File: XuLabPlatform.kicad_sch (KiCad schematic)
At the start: 0 parts

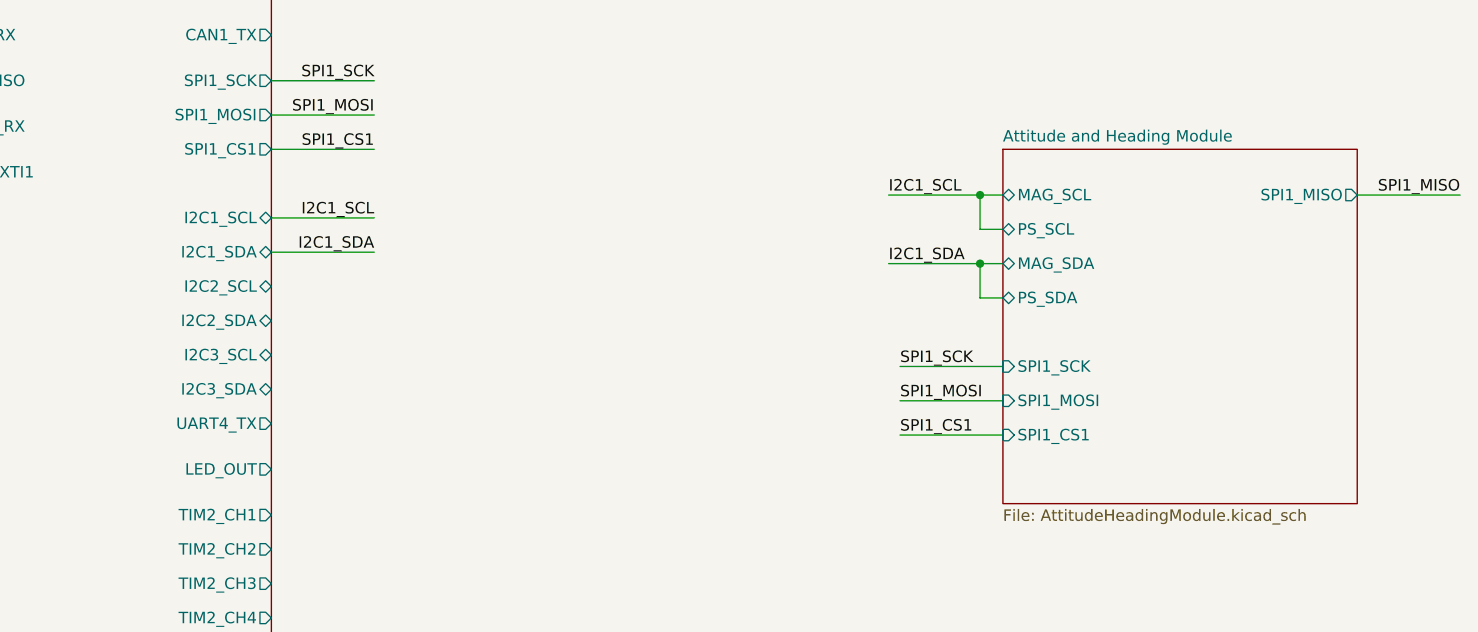
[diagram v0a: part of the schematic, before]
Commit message: Change magnetometer interface from I2C to SPI
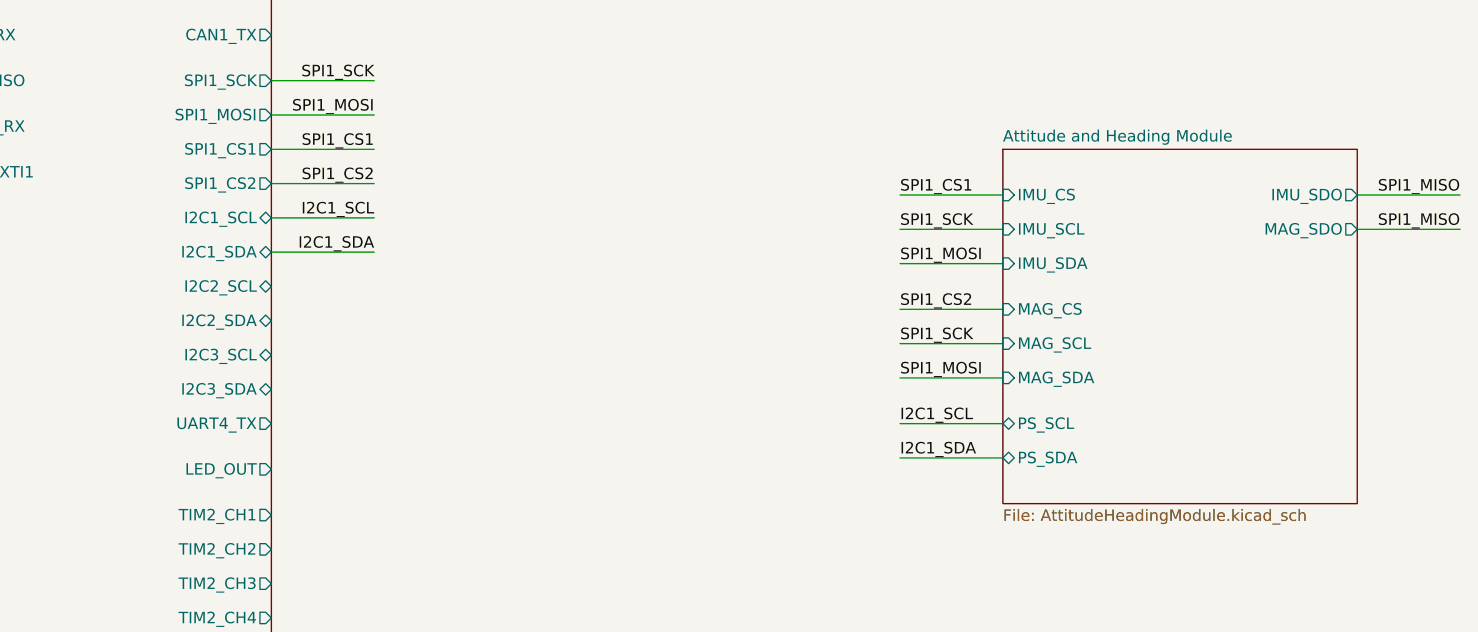
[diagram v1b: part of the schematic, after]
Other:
- sheet Attitude and Heading Module ports: added IMU_CS, IMU_SCL, IMU_SDA, IMU_SDO, MAG_CS, MAG_SDO; removed SPI1_CS1, SPI1_MISO, SPI1_MOSI, SPI1_SCK
- sheet MCU A ports: added SPI1_CS2; removed none
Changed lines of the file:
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@@
 	(title_block
 		(title "Main Sheet")
-		(date "2025-10-21")
+		(date "2025-10-23")
 		(rev "A")
 		(company "CU Boulder Senior Design Team 29 - Xu Lab")
 	)
-	(junction
-		(at 167.64 60.96)
-		(diameter 0)
-		(color 0 0 0 0)
-	)
-	(junction
-		(at 167.64 68.58)
-		(diameter 0)
-		(color 0 0 0 0)
+	(wire
+		(pts
+			(xy 158.75 64.77) (xy 170.18 64.77)
+		)
+		(stroke
+			(width 0)
+			(type default)
+		)
 	)
 	(wire
@@
 	(wire
 		(pts
+			(xy 209.55 64.77) (xy 220.98 64.77)
+		)
+		(stroke
+			(width 0)
+			(type default)
+		)
+	)
+	(wire
+		(pts
 			(xy 88.9 48.26) (xy 100.33 48.26)
 		)
@@
 	(wire
 		(pts
-			(xy 167.64 68.58) (xy 170.18 68.58)
-		)
-		(stroke
-			(width 0)
-			(type default)
-		)
-	)
-	(wire
-		(pts
-			(xy 170.18 72.39) (xy 167.64 72.39)
+			(xy 158.75 73.66) (xy 170.18 73.66)
 		)
 		(stroke
@@
 	(wire
 		(pts
-			(xy 170.18 64.77) (xy 167.64 64.77)
-		)
-		(stroke
-			(width 0)
-			(type default)
-		)
-	)
-	(wire
-		(pts
-			(xy 158.75 83.82) (xy 170.18 83.82)
-		)
-		(stroke
-			(width 0)
-			(type default)
-		)
-	)
-	(wire
-		(pts
-			(xy 167.64 60.96) (xy 167.64 64.77)
+			(xy 158.75 60.96) (xy 170.18 60.96)
+		)
+		(stroke
+			(width 0)
+			(type default)
+		)
+	)
+	(wire
+		(pts
+			(xy 158.75 68.58) (xy 170.18 68.58)
+		)
+		(stroke
+			(width 0)
+			(type default)
+		)
+	)
+	(wire
+		(pts
+			(xy 158.75 77.47) (xy 170.18 77.47)
 		)
 		(stroke
@@
 	(wire
 		(pts
-			(xy 158.75 80.01) (xy 170.18 80.01)
+			(xy 88.9 59.69) (xy 100.33 59.69)
 		)
 		(stroke
@@
 	(wire
 		(pts
-			(xy 157.48 60.96) (xy 167.64 60.96)
-		)
-		(stroke
-			(width 0)
-			(type default)
-		)
-	)
-	(wire
-		(pts
-			(xy 158.75 87.63) (xy 170.18 87.63)
-		)
-		(stroke
-			(width 0)
-			(type default)
-		)
-	)
-	(wire
-		(pts
-			(xy 157.48 68.58) (xy 167.64 68.58)
-		)
-		(stroke
-			(width 0)
-			(type default)
-		)
-	)
-	(wire
-		(pts
-			(xy 167.64 60.96) (xy 170.18 60.96)
-		)
-		(stroke
-			(width 0)
-			(type default)
-		)
-	)
-	(wire
-		(pts
 			(xy 209.55 60.96) (xy 220.98 60.96)
 		)
@@
 	(wire
 		(pts
-			(xy 167.64 68.58) (xy 167.64 72.39)
+			(xy 158.75 81.28) (xy 170.18 81.28)
+		)
+		(stroke
+			(width 0)
+			(type default)
+		)
+	)
+	(wire
+		(pts
+			(xy 158.75 90.17) (xy 170.18 90.17)
 		)
 		(stroke
@@
 		)
 	)
-	(label "SPI1_CS1"
-		(at 158.75 87.63 0)
-		(effects
-			(font
-				(size 1.27 1.27)
-			)
-			(justify left bottom)
+	(wire
+		(pts
+			(xy 158.75 86.36) (xy 170.18 86.36)
+		)
+		(stroke
+			(width 0)
+			(type default)
+		)
+	)
+	(label "SPI1_MOSI"
+		(at 158.75 81.28 0)
+		(effects
+			(font
+				(size 1.27 1.27)
+			)
+			(justify left bottom)
+		)
+	)
+	(label "SPI1_MISO"
+		(at 220.98 60.96 180)
+		(effects
+			(font
+				(size 1.27 1.27)
+			)
+			(justify right bottom)
 		)
 	)
@@
 	)
 	(label "SPI1_MISO"
-		(at 220.98 60.96 180)
+		(at 220.98 64.77 180)
 		(effects
 			(font
@@
 			)
 			(justify right bottom)
-		)
-	)
-	(label "I2C1_SDA"
-		(at 157.48 68.58 0)
-		(effects
-			(font
-				(size 1.27 1.27)
-			)
-			(justify left bottom)
 		)
 	)
@@
 		)
 	)
+	(label "SPI1_SCK"
+		(at 158.75 77.47 0)
+		(effects
+			(font
+				(size 1.27 1.27)
+			)
+			(justify left bottom)
+		)
+	)
 	(label "SPI1_MOSI"
 		(at 100.33 52.07 180)
@@
 		)
 	)
+	(label "SPI1_SCK"
+		(at 158.75 64.77 0)
+		(effects
+			(font
+				(size 1.27 1.27)
+			)
+			(justify left bottom)
+		)
+	)
+	(label "SPI1_CS1"
+		(at 158.75 60.96 0)
+		(effects
+			(font
+				(size 1.27 1.27)
+			)
+			(justify left bottom)
+		)
+	)
 	(label "I2C1_SCL"
-		(at 157.48 60.96 0)
-		(effects
-			(font
-				(size 1.27 1.27)
-			)
-			(justify left bottom)
+		(at 158.75 86.36 0)
+		(effects
+			(font
+				(size 1.27 1.27)
+			)
+			(justify left bottom)
+		)
+	)
+	(label "SPI1_CS2"
+		(at 100.33 59.69 180)
+		(effects
+			(font
+				(size 1.27 1.27)
+			)
+			(justify right bottom)
 		)
 	)
@@
 		)
 	)
+	(label "SPI1_CS2"
+		(at 158.75 73.66 0)
+		(effects
+			(font
+				(size 1.27 1.27)
+			)
+			(justify left bottom)
+		)
+	)
+	(label "I2C1_SDA"
+		(at 158.75 90.17 0)
+		(effects
+			(font
+				(size 1.27 1.27)
+			)
+			(justify left bottom)
+		)
+	)
 	(label ""
 		(at 97.79 48.26 0)
@@
 	)
 	(label "SPI1_SCK"
-		(at 158.75 80.01 0)
-		(effects
-			(font
-				(size 1.27 1.27)
-			)
-			(justify left bottom)
-		)
-	)
-	(label "SPI1_SCK"
 		(at 100.33 48.26 180)
 		(effects
@@
 	)
 	(label "SPI1_MOSI"
-		(at 158.75 83.82 0)
+		(at 158.75 68.58 0)
 		(effects
 			(font
@@
 			)
 		)
+		(pin "SPI1_CS2" output
+			(at 88.9 59.69 0)
+			(effects
+				(font
+					(size 1.27 1.27)
+				)
+				(justify right)
+			)
+		)
 		(instances
 			(project "XuLabPlatform"
@@
 			)
 		)
-		(pin "MAG_SCL" bidirectional
+		(pin "IMU_CS" input
 			(at 170.18 60.96 180)
 			(effects
@@
 			)
 		)
-		(pin "MAG_SDA" bidirectional
+		(pin "IMU_SCL" input
+			(at 170.18 64.77 180)
+			(effects
+				(font
+					(size 1.27 1.27)
+				)
+				(justify left)
+			)
+		)
+		(pin "IMU_SDA" input
 			(at 170.18 68.58 180)
 			(effects
@@
 			)
 		)
-		(pin "SPI1_CS1" input
-			(at 170.18 87.63 180)
-			(effects
-				(font
-					(size 1.27 1.27)
-				)
-				(justify left)
-			)
-		)
-		(pin "SPI1_MISO" output
+		(pin "IMU_SDO" output
 			(at 209.55 60.96 0)
 			(effects
@@
 			)
 		)
-		(pin "SPI1_MOSI" input
-			(at 170.18 83.82 180)
-			(effects
-				(font
-					(size 1.27 1.27)
-				)
-				(justify left)
-			)
-		)
-		(pin "SPI1_SCK" input
-			(at 170.18 80.01 180)
-			(effects
-				(font
-					(size 1.27 1.27)
-				)
-				(justify left)
+		(pin "MAG_CS" input
+			(at 170.18 73.66 180)
+			(effects
+				(font
+					(size 1.27 1.27)
+				)
+				(justify left)
+			)
+		)
+		(pin "MAG_SCL" input
+			(at 170.18 77.47 180)
+			(effects
+				(font
+					(size 1.27 1.27)
+				)
+				(justify left)
+			)
+		)
+		(pin "MAG_SDA" input
+			(at 170.18 81.28 180)
+			(effects
+				(font
+					(size 1.27 1.27)
+				)
+				(justify left)
+			)
+		)
+		(pin "MAG_SDO" output
+			(at 209.55 64.77 0)
+			(effects
+				(font
+					(size 1.27 1.27)
+				)
+				(justify right)
 			)
 		)
 		(pin "PS_SCL" bidirectional
-			(at 170.18 64.77 180)
+			(at 170.18 86.36 180)
 			(effects
 				(font
@@
 		)
 		(pin "PS_SDA" bidirectional
-			(at 170.18 72.39 180)
-			(effects
-				(font
+			(at 170.18 90.17 180)
+			(effects
+				(font

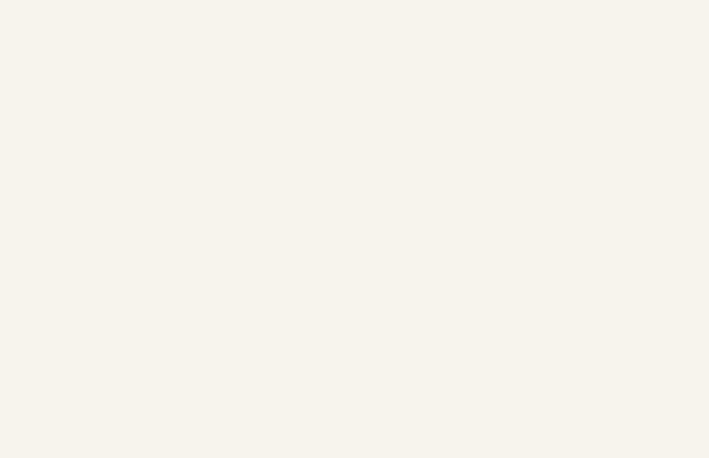
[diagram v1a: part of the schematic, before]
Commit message: Add power schematic sheet
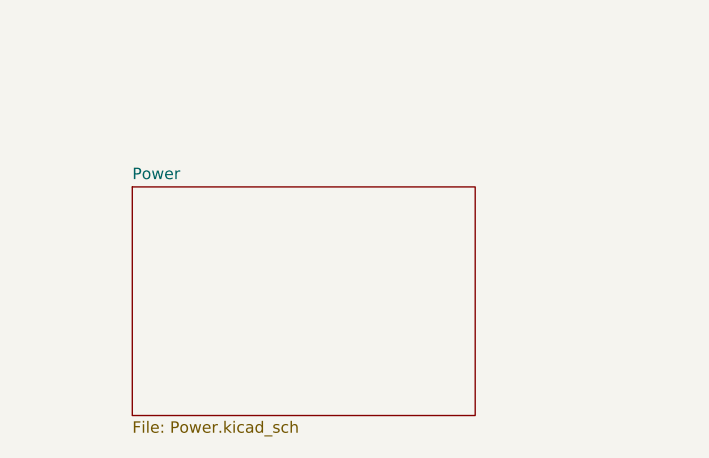
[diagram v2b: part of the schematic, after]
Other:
- added sheet Power (Power.kicad_sch)
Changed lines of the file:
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@@
+	)
+	(sheet
+		(at 50.8 152.4)
+		(size 38.1 25.4)
+		(exclude_from_sim no)
+		(in_bom yes)
+		(on_board yes)
+		(dnp no)
+		(fields_autoplaced yes)
+		(stroke
+			(width 0.1524)
+			(type solid)
+		)
+		(fill
+			(color 0 0 0 0.0000)
+		)
+		(property "Sheetname" "Power"
+			(at 50.8 151.6884 0)
+			(effects
+				(font
+					(size 1.27 1.27)
+				)
+				(justify left bottom)
+			)
+		)
+		(property "Sheetfile" "Power.kicad_sch"
+			(at 50.8 178.3846 0)
+			(effects
+				(font
+					(size 1.27 1.27)
+				)
+				(justify left top)
+			)
+		)
+		(instances
+			(project "XuLabPlatform"
+				(path "/71bb14ae-b730-4d22-a41d-cf68989dae2d"
+					(page "4")
+				)
+			)
+		)
 	)
 	(sheet

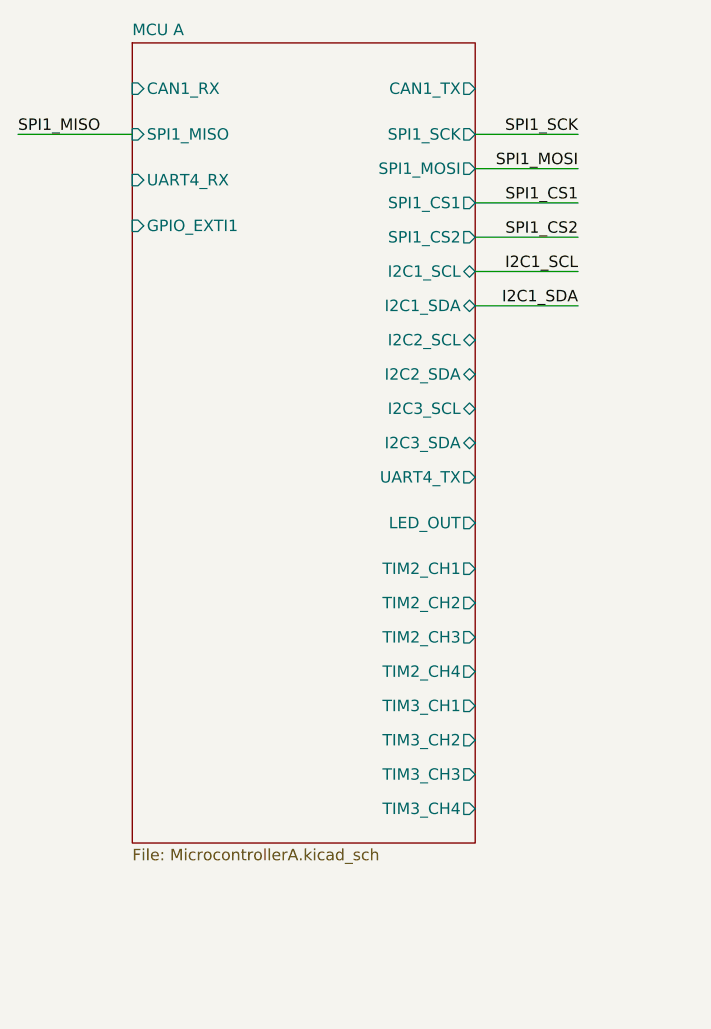
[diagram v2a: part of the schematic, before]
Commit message: Add indicator LED for MCU A
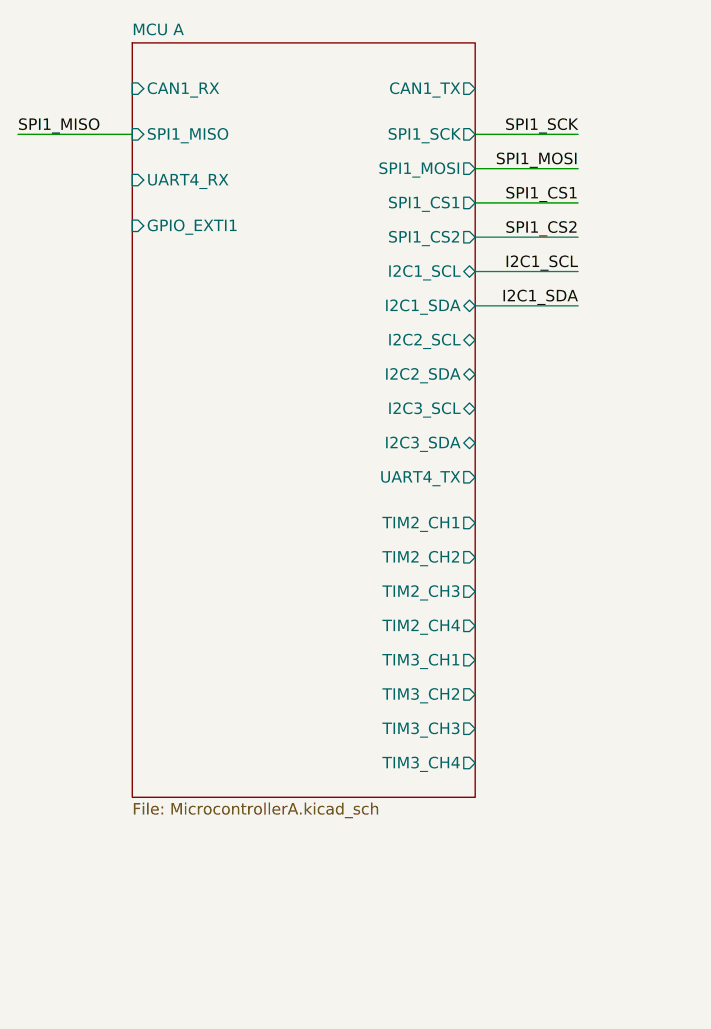
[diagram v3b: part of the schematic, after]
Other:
- sheet MCU A ports: added none; removed LED_OUT
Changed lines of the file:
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@@
 	(sheet
 		(at 50.8 38.1)
-		(size 38.1 88.9)
+		(size 38.1 83.82)
 		(exclude_from_sim no)
 		(in_bom yes)
@@
 		)
 		(property "Sheetfile" "MicrocontrollerA.kicad_sch"
-			(at 50.8 127.5846 0)
+			(at 50.8 122.5046 0)
 			(effects
 				(font
@@
 		)
 		(pin "TIM2_CH1" output
-			(at 88.9 96.52 0)
+			(at 88.9 91.44 0)
 			(effects
 				(font
@@
 		)
 		(pin "TIM2_CH2" output
-			(at 88.9 100.33 0)
+			(at 88.9 95.25 0)
 			(effects
 				(font
@@
 		)
 		(pin "TIM2_CH3" output
-			(at 88.9 104.14 0)
+			(at 88.9 99.06 0)
 			(effects
 				(font
@@
 		)
 		(pin "TIM2_CH4" output
-			(at 88.9 107.95 0)
+			(at 88.9 102.87 0)
 			(effects
 				(font
@@
 		)
 		(pin "TIM3_CH1" output
-			(at 88.9 111.76 0)
+			(at 88.9 106.68 0)
 			(effects
 				(font
@@
 		)
 		(pin "TIM3_CH2" output
-			(at 88.9 115.57 0)
+			(at 88.9 110.49 0)
 			(effects
 				(font
@@
 		)
 		(pin "TIM3_CH3" output
-			(at 88.9 119.38 0)
+			(at 88.9 114.3 0)
 			(effects
 				(font
@@
 		)
 		(pin "TIM3_CH4" output
-			(at 88.9 123.19 0)
+			(at 88.9 118.11 0)
 			(effects
 				(font
@@
 			(effects
 				(font
-					(size 1.27 1.27)
-				)
-				(justify right)
-			)
-		)
-		(pin "LED_OUT" output
-			(at 88.9 91.44 0)
-			(effects
-				(font
